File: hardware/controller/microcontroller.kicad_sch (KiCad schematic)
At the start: 41 parts, among them J1 USB_C_Receptacle_USB2.0_14P, J2 IDC-10, SW1 SW_Push, SW2 SW_Push, SW3 SW_Push, U1 SRV05-4, U2 ESP32-C3-WROOM-02, U3 STM32U535RET6, U4 nRF24L01+ 2.4Gz Mini SMD, Y1 8MHz

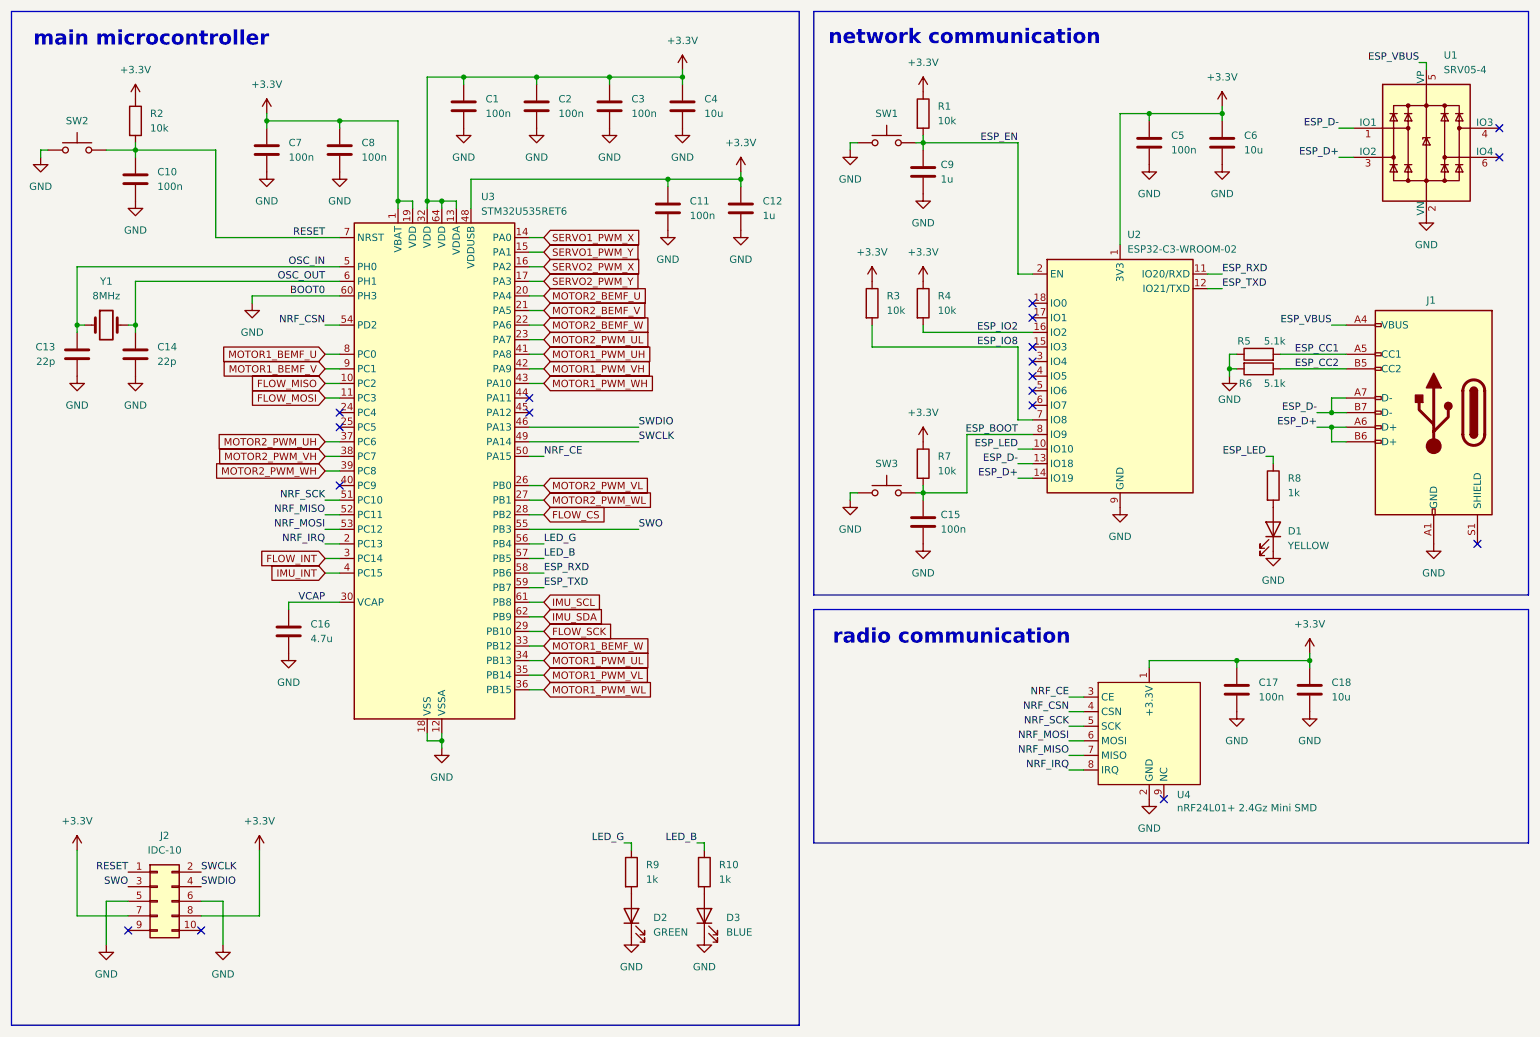
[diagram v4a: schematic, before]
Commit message: add VBUS sense to STM and ESP, change buttons and sw to vertical, add USB-C to SEM
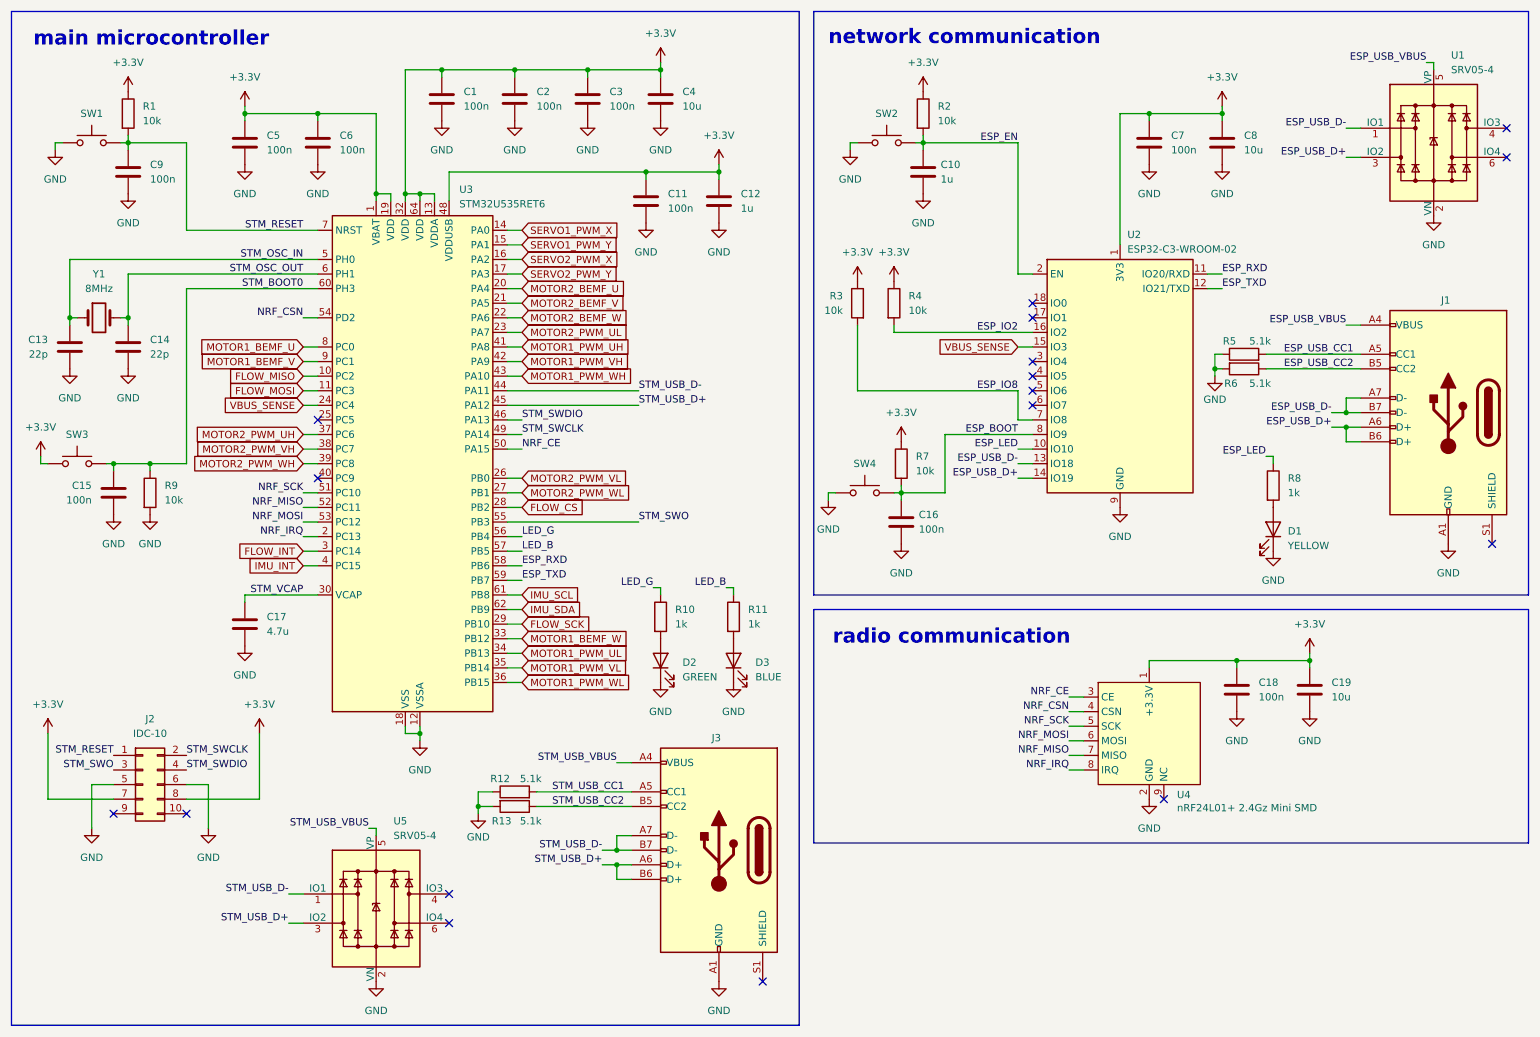
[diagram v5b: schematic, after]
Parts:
- added C15: 100n, Capacitor_SMD:C_0603_1608Metric, symbol Device:C
- added J3: USB_C_Receptacle_USB2.0_14P, Connector_USB:USB_C_Receptacle_GCT_USB4085, symbol Connector:USB_C_Receptacle_USB2.0_14P
- added R12, R13: 5.1k, Resistor_SMD:R_0603_1608Metric, symbol Device:R
- added R9: 10k, Resistor_SMD:R_0603_1608Metric, symbol Device:R
- added SW3: SW_Push, Button_Switch_SMD:SW_SPST_CK_RS282G05A3, symbol Switch:SW_Push
- added U5: SRV05-4, Package_TO_SOT_SMD:SOT-23-6, symbol Power_Protection:SRV05-4
- J2: footprint Connector_IDC:IDC-Header_2x05_P2.54mm_Horizontal -> Connector_IDC:IDC-Header_2x05_P2.54mm_Vertical
- SW1: renamed from SW2; footprint Button_Switch_THT:SW_Tactile_SPST_Angled_PTS645Vx58-2LFS -> Button_Switch_SMD:SW_SPST_CK_RS282G05A3
- SW2: renamed from SW1; footprint Button_Switch_THT:SW_Tactile_SPST_Angled_PTS645Vx58-2LFS -> Button_Switch_SMD:SW_SPST_CK_RS282G05A3
- SW4: renamed from SW3; footprint Button_Switch_THT:SW_Tactile_SPST_Angled_PTS645Vx58-2LFS -> Button_Switch_SMD:SW_SPST_CK_RS282G05A3
- renumbered C9 to C10, C15 to C16, C16 to C17, C17 to C18, C18 to C19, C7 to C5, C8 to C6, C5 to C7, C6 to C8, C10 to C9, R2 to R1, R9 to R10, R10 to R11, R1 to R2
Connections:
- net +3.3V: now also SW3.1
- net GND: now also C15.2, J3.A1 (GND), J3.A12 (GND), J3.B1 (GND), J3.B12 (GND), R12.1, R13.2, R9.2, U5.2 (VN); no longer U3.60 (PH3)
- net VBUS_SENSE: now reaches U2.15 (IO3)
- net VBUS_SENSE: now also U3.24 (PC4)
- net STM_USB_D-: now reaches U3.44 (PA11)
- net STM_USB_D-: now also J3.A7 (D-), J3.B7 (D-), U5.1 (IO1)
- net STM_USB_D+: now reaches U3.45 (PA12)
- net STM_USB_D+: now also J3.A6 (D+), J3.B6 (D+), U5.3 (IO2)
- net ESP_CC1 renamed ESP_USB_CC1
- net ESP_CC2 renamed ESP_USB_CC2
- net ESP_D+ renamed ESP_USB_D+
- net ESP_D- renamed ESP_USB_D-
- net ESP_VBUS renamed ESP_USB_VBUS
- net OSC_IN renamed STM_OSC_IN
- net OSC_OUT renamed STM_OSC_OUT
- net RESET renamed STM_RESET
- net SWCLK renamed STM_SWCLK
- net SWDIO renamed STM_SWDIO
- net SWO renamed STM_SWO
- net VCAP renamed STM_VCAP
- new net STM_BOOT0: C15.1, R9.1, SW3.2, U3.60 (PH3)
- new net STM_USB_CC1: J3.A5 (CC1), R12.2
- new net STM_USB_CC2: J3.B5 (CC2), R13.1
- new net STM_USB_VBUS: J3.A4 (VBUS), J3.A9 (VBUS), J3.B4 (VBUS), J3.B9 (VBUS), U5.5 (VP)
- no-connect marks 18 -> 17
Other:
- moved on the sheet: C1, C11, C12, C13, C14, C16, C17, C2, C3, C4, C5, C6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

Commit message: USBLC6, IR2101
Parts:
- removed U1, U5: SRV05-4, Package_TO_SOT_SMD:SOT-23-6, symbol Power_Protection:SRV05-4
- added U1, U5: USBLC6-2SC6, Package_TO_SOT_SMD:SOT-23-6, symbol Power_Protection:USBLC6-2SC6
- renumbered C8 to C11, C7 to C12, C9 to C7, C11 to C8, C12 to C9, R5 to R1, R6 to R2, R1 to R3, R2 to R4, R3 to R5, R4 to R6, R8 to R7, R7 to R8
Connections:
- net ESP_USB_D+: now also U1.3 (I/O2); no longer J1.A6 (D+), J1.B6 (D+)
- net ESP_USB_D-: now also U1.1 (I/O1); no longer J1.A7 (D-), J1.B7 (D-)
- net ESP_USB_VBUS: now also U1.5 (VBUS)
- net GND: now also U1.2 (GND), U5.2 (GND)
- net STM_USB_D+: now also U5.3 (I/O2); no longer J3.A6 (D+), J3.B6 (D+)
- net STM_USB_D-: now also U5.1 (I/O1); no longer J3.A7 (D-), J3.B7 (D-)
- net STM_USB_VBUS: now also U5.5 (VBUS)
- new net: J1.A6 (D+), J1.B6 (D+), U1.4 (I/O2)
- new net: J1.A7 (D-), J1.B7 (D-), U1.6 (I/O1)
- new net: J3.A6 (D+), J3.B6 (D+), U5.4 (I/O2)
- new net: J3.A7 (D-), J3.B7 (D-), U5.6 (I/O1)
- no-connect marks 17 -> 13
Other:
- moved on the sheet: C10, C11, C12, C16, D1, J1, R1, R2, R4, R5, R6, R7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

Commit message: custom footprints with all 3D models
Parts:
- SW1, SW2, SW3, SW4: footprint Button_Switch_SMD:SW_SPST_CK_RS282G05A3 -> hogger2:spst_6x3mm
- U4: footprint (none) -> hogger2:nRF24L01p_Mini_SMD
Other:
- moved on the sheet: R6
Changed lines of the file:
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@@
 	(wire
 		(pts
-			(xy 171.45 46.99) (xy 182.88 46.99)
+			(xy 171.45 46.99) (xy 180.34 46.99)
 		)
 		(stroke
@@
 	(wire
 		(pts
-			(xy 170.18 80.01) (xy 170.18 78.74)
+			(xy 171.45 80.01) (xy 171.45 78.74)
 		)
 		(stroke
@@
 	(wire
 		(pts
-			(xy 182.88 46.99) (xy 182.88 69.85)
+			(xy 180.34 46.99) (xy 180.34 69.85)
 		)
 		(stroke
@@
 	(wire
 		(pts
-			(xy 170.18 80.01) (xy 194.31 80.01)
+			(xy 171.45 80.01) (xy 194.31 80.01)
 		)
 		(stroke
@@
 	(wire
 		(pts
-			(xy 182.88 69.85) (xy 194.31 69.85)
+			(xy 180.34 69.85) (xy 194.31 69.85)
 		)
 		(stroke
@@
 	(symbol
 		(lib_id "power:+3.3V")
-		(at 170.18 71.12 0)
+		(at 171.45 71.12 0)
 		(unit 1)
 		(exclude_from_sim no)
@@
 		(fields_autoplaced yes)
 		(property "Reference" "#PWR026"
-			(at 170.18 74.93 0)
+			(at 171.45 74.93 0)
 			(effects
 				(font
@@
 		)
 		(property "Value" "+3.3V"
-			(at 170.18 66.04 0)
+			(at 171.45 66.04 0)
 			(effects
 				(font
@@
 		)
 		(property "Footprint" ""
-			(at 170.18 71.12 0)
+			(at 171.45 71.12 0)
 			(effects
 				(font
@@
 		)
 		(property "Datasheet" ""
-			(at 170.18 71.12 0)
+			(at 171.45 71.12 0)
 			(effects
 				(font
@@
 		)
 		(property "Description" "Power symbol creates a global label with name \"+3.3V\""
-			(at 170.18 71.12 0)
+			(at 171.45 71.12 0)
 			(effects
 				(font
@@
 	(symbol
 		(lib_id "Device:R")
-		(at 170.18 74.93 0)
+		(at 171.45 74.93 0)
 		(unit 1)
 		(exclude_from_sim no)
@@
 		(dnp no)
 		(property "Reference" "R6"
-			(at 172.72 73.6599 0)
+			(at 173.99 73.6599 0)
 			(effects
 				(font
@@
 		)
 		(property "Value" "10k"
-			(at 172.72 76.1999 0)
+			(at 173.99 76.1999 0)
 			(effects
 				(font
@@
 		)
 		(property "Footprint" "Resistor_SMD:R_0603_1608Metric"
-			(at 168.402 74.93 90)
+			(at 169.672 74.93 90)
 			(effects
 				(font
@@
 		)
 		(property "Datasheet" "~"
-			(at 170.18 74.93 0)
+			(at 171.45 74.93 0)
 			(effects
 				(font
@@
 		)
 		(property "Description" "Resistor"
-			(at 170.18 74.93 0)
+			(at 171.45 74.93 0)
 			(effects
 				(font
@@
 			)
 		)
-		(property "Footprint" "Button_Switch_SMD:SW_SPST_CK_RS282G05A3"
+		(property "Footprint" "hogger2:spst_6x3mm"
 			(at 30.48 34.29 0)
 			(effects
@@
 			)
 		)
-		(property "Footprint" "Button_Switch_SMD:SW_SPST_CK_RS282G05A3"
+		(property "Footprint" "hogger2:spst_6x3mm"
 			(at 165.1 96.52 0)
 			(effects
@@
 			)
 		)
-		(property "Footprint" "Button_Switch_SMD:SW_SPST_CK_RS282G05A3"
+		(property "Footprint" "hogger2:spst_6x3mm"
 			(at 27.94 90.17 0)
 			(effects
@@
 			)
 		)
-		(property "Footprint" ""
+		(property "Footprint" "hogger2:nRF24L01p_Mini_SMD"
 			(at 214.63 140.97 0)
 			(effects
@@
 			)
 		)
-		(property "Footprint" "Button_Switch_SMD:SW_SPST_CK_RS282G05A3"
+		(property "Footprint" "hogger2:spst_6x3mm"
 			(at 165.1 41.91 0)
 			(effects

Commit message: back to LM2105, remove USB-C from STM
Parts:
- removed C15: 100n, Capacitor_SMD:C_0603_1608Metric, symbol Device:C
- removed D2: GREEN, LED_SMD:LED_0603_1608Metric, symbol Device:LED
- removed J3: USB_C_Receptacle_USB2.0_14P, Connector_USB:USB_C_Receptacle_GCT_USB4085, symbol Connector:USB_C_Receptacle_USB2.0_14P
- removed R10: 1k, Resistor_SMD:R_0603_1608Metric, symbol Device:R
- removed R12, R13: 5.1k, Resistor_SMD:R_0603_1608Metric, symbol Device:R
- removed R9: 10k, Resistor_SMD:R_0603_1608Metric, symbol Device:R
- removed SW3: SW_Push, hogger2:spst_6x3mm, symbol Switch:SW_Push
- removed U5: USBLC6-2SC6, Package_TO_SOT_SMD:SOT-23-6, symbol Power_Protection:USBLC6-2SC6
- renumbered C5 to C1, C16 to C15, C17 to C16, C18 to C17, C19 to C18, C6 to C2, C1 to C3, C2 to C4, C3 to C5, C4 to C6, D3 to D2, R11 to R9, SW4 to SW3
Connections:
- net STM_BOOT0 is gone; now on net GND: U3.60 (PH3)
- net FLOW_CS: now also U3.25 (PC5); no longer U3.28 (PB2)
- net MOTOR1_BEMF_W: now also U3.28 (PB2); no longer U3.33 (PB12)
- net LED_B renamed STM_LED
- net LED_G: no longer names the net of U3.56 (PB4)
- net STM_USB_D+: no longer names the net of U3.45 (PA12)
- net STM_USB_D-: no longer names the net of U3.44 (PA11)
- no-connect marks 13 -> 15
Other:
- moved on the sheet: C1, C16, C2, C3, C4, C5, C6, C7, C8, C9, D2, J2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
